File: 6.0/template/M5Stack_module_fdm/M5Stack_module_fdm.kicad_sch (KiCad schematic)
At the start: 9 parts, among them U1 M-BUS

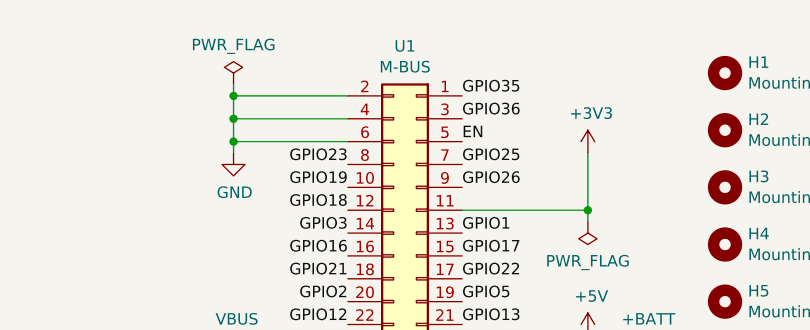
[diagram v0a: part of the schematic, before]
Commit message: template M5Stack
M-BUS connector  U1 to J1
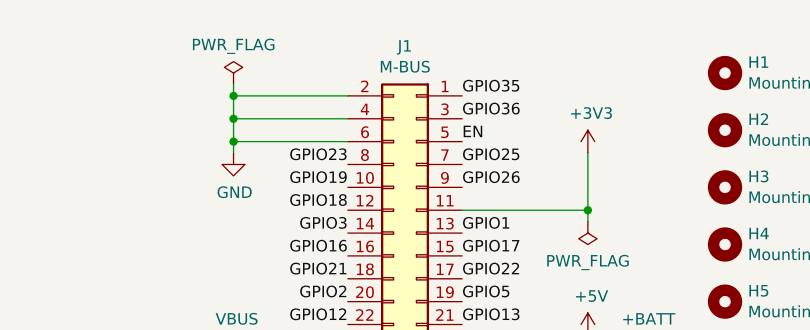
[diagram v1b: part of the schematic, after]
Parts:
- renumbered U1 to J1
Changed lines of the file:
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@@
   (paper "A4")
   (title_block
-    (date "2022-10-22")
+    (date "2022-10-23")
   )
   (junction (at 212.09 21.59) (diameter 0) (color 0 0 0 0)
@@
   (symbol (lib_id "Connector_Generic:Conn_02x15_Odd_Even") (at 232.41 39.37 0) (mirror y) (unit 1)
     (in_bom yes) (on_board yes)
-    (property "Reference" "U1" (id 0) (at 231.14 16.0782 0))
+    (property "Reference" "J1" (id 0) (at 231.14 16.0782 0))
     (property "Value" "M-BUS" (id 1) (at 231.14 18.3896 0))
     (property "Footprint" "@bf:BF@M5Stack_MBUS" (id 2) (at 232.41 39.37 0)
@@
     )
     (path "/f53ca6a9-a3d5-4b49-96ba-0af877934a36"
-      (reference "U1") (unit 1) (value "M-BUS") (footprint "@bf:BF@M5Stack_MBUS")
+      (reference "J1") (unit 1) (value "M-BUS") (footprint "@bf:BF@M5Stack_MBUS")
     )
   )
